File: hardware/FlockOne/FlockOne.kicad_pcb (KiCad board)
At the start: 2 copper layers, 17 x 21.5 mm, 14 parts, among them J1 Port, J2 Programming, U1 MIC5219-3.3YM5, U2 STM32F030F4P6, U3 AITHINKER-RA02

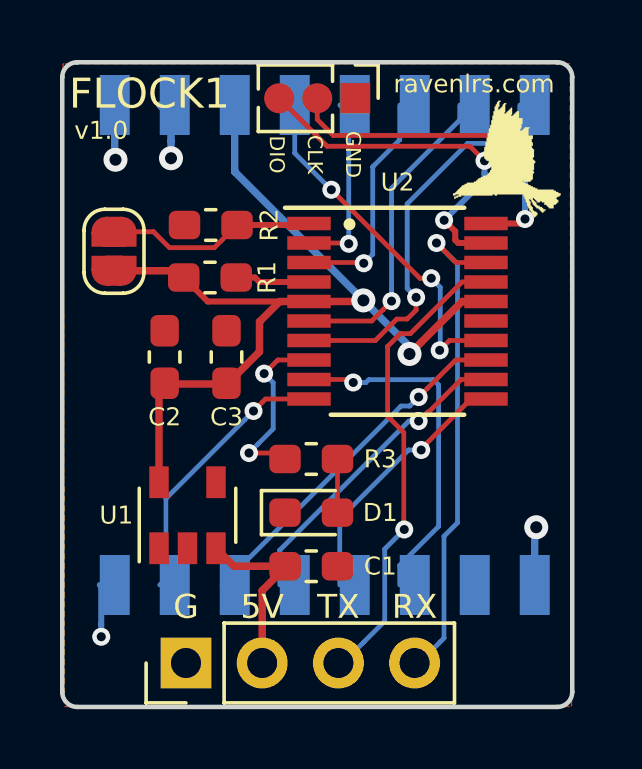
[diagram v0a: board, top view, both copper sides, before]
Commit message: Fix missing connection to the EN pin on MIC5219
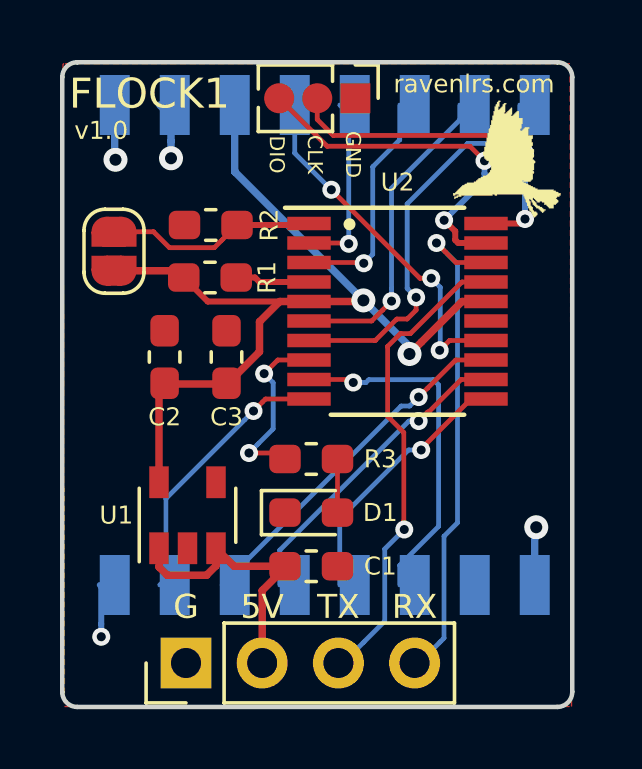
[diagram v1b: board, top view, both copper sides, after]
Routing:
- net +5V: track 6.16 -> 9.51 mm
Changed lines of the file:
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@@
     (thickness 1.6)
     (drawings 31)
-    (tracks 194)
+    (tracks 199)
     (zones 0)
     (modules 14)
@@
   (segment (start 155.725 78.6) (end 155.125 78) (width 0.25) (layer F.Cu) (net 2))
   (segment (start 157.475 78.6) (end 155.725 78.6) (width 0.25) (layer F.Cu) (net 2))
+  (segment (start 154.810002 78.9) (end 155.125 78.585002) (width 0.25) (layer F.Cu) (net 2))
+  (segment (start 155.125 78.585002) (end 155.125 78) (width 0.25) (layer F.Cu) (net 2))
+  (segment (start 153.5 78.9) (end 154.810002 78.9) (width 0.25) (layer F.Cu) (net 2))
+  (segment (start 153.225 78.625) (end 153.5 78.9) (width 0.25) (layer F.Cu) (net 2))
+  (segment (start 153.225 78) (end 153.225 78.625) (width 0.25) (layer F.Cu) (net 2))
   (segment (start 155.45 72.525) (end 155.475 72.55) (width 0.25) (layer F.Cu) (net 3))
   (segment (start 153.35 72.525) (end 155.45 72.525) (width 0.25) (layer F.Cu) (net 3))

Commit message: Move DIO5 to HSE bypass input
This lets use use the xtal in the LoRa module as HSE rather than
using it for trimming HSI.
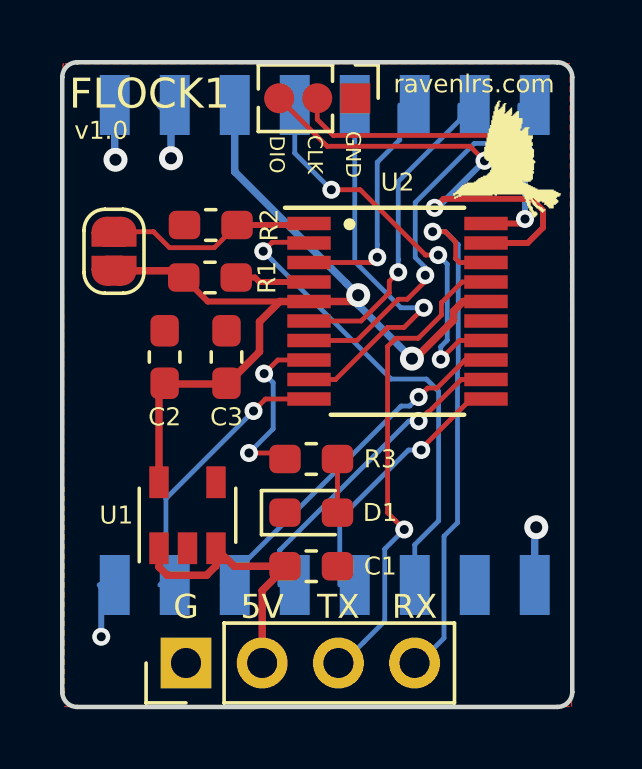
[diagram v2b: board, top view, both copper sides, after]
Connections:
- U2 pad 2: DIO0 -> DIO5
- U2 pad 9: DIO5 -> DIO0
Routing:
- net DIO0: track 6.08 -> 13.0 mm
- net DIO5: track 11.7 -> 16.2 mm
- net SWDIO: track 12.1 -> 16.6 mm
- net RX: track 17.0 -> 18.3 mm
- net RESET: track 12.1 -> 13.3 mm
